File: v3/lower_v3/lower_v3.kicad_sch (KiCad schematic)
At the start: 4 parts, among them J1 Conn_01x09_MountingPin, J2 Conn_01x09_MountingPin, J4 Conn_01x02_Male, U1 ESP32-DEVKIT-V1

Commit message: Updates
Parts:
- added N1: Housing, Filter:Filter_1109-5_1.1x0.9mm, symbol Mechanical:Housing
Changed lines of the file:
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@@
     (pin "2")
+  )
+  (symbol (lib_id "Mechanical:Housing") (at 194.31 96.52 0) (unit 1)
+    (in_bom yes) (on_board yes) (fields_autoplaced)
+    (property "Reference" "N1" (id 0) (at 198.12 95.5674 0)
+      (effects (font (size 1.27 1.27)) (justify left))
+    )
+    (property "Value" "Housing" (id 1) (at 198.12 98.1074 0)
+      (effects (font (size 1.27 1.27)) (justify left))
+    )
+    (property "Footprint" "Filter:Filter_1109-5_1.1x0.9mm" (id 2) (at 195.58 95.25 0)
+      (effects (font (size 1.27 1.27)) hide)
+    )
+    (property "Datasheet" "~" (id 3) (at 195.58 95.25 0)
+      (effects (font (size 1.27 1.27)) hide)
+    )
   )
   (sheet_instances
@@
       (reference "J4") (unit 1) (value "Conn_01x02_Male") (footprint "Connector_PinHeader_2.54mm:PinHeader_1x02_P2.54mm_Vertical")
     )
+    (path "/b4f93f89-84ab-4a49-afa5-fdb220e94526"
+      (reference "N1") (unit 1) (value "Housing") (footprint "Filter:Filter_1109-5_1.1x0.9mm")
+    )
     (path "/821c0c0e-bb45-4cb0-9a8b-2228365f0032"

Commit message: Complete Toast PCB
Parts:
- removed J1, J2: Conn_01x09_MountingPin, Connector_PinSocket_2.54mm:PinSocket_1x09_P2.54mm_Vertical, symbol Connector_Generic_MountingPin:Conn_01x09_MountingPin
- added J1, J2: Conn_01x05_Male, Connector_PinHeader_2.54mm:PinHeader_1x05_P2.54mm_Vertical, symbol Connector:Conn_01x05_Male
- added J3: Conn_01x21, Connector_PinHeader_2.54mm:PinHeader_1x21_P2.54mm_Horizontal, symbol Connector_Generic:Conn_01x21
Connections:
- net GND: now also J4.2 (Pin_2), J2.1 (Pin_1), J3.12 (Pin_12), J3.15 (Pin_15), J3.18 (Pin_18), J3.21 (Pin_21), J3.3 (Pin_3), J3.6 (Pin_6), J3.9 (Pin_9); no longer J4.1 (Pin_1)
- net at U1.11 (D21): now also J1.1 (Pin_1)
- net at U1.10 (D19): now also J1.2 (Pin_2)
- net at U1.9 (D18): now also J1.3 (Pin_3)
- net at U1.8 (D5): now also J1.4 (Pin_4)
- net at U1.5 (D4): now also J2.4 (Pin_4)
- net at U1.4 (D2): now also J2.5 (Pin_5)
- net at U1.28 (D13): now also J2.2 (Pin_2)
- net at U1.27 (D12): now also J2.3 (Pin_3)
- net at U1.30 (VIN): now also J1.5 (Pin_5)
- net at U1.19 (D34): now also J3.19 (Pin_19)
- net at U1.20 (D35): now also J3.16 (Pin_16)
- net at U1.21 (D32): now also J3.13 (Pin_13)
- net at U1.22 (D33): now also J3.10 (Pin_10)
- net at U1.23 (D25): now also J3.7 (Pin_7)
- net at U1.25 (D27): now also J3.4 (Pin_4)
- net at U1.26 (D14): now also J3.1 (Pin_1)
- new net: J3.11 (Pin_11), J3.14 (Pin_14), J3.17 (Pin_17), J3.2 (Pin_2), J3.20 (Pin_20), J3.5 (Pin_5), J3.8 (Pin_8), J4.1 (Pin_1)
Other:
- moved on the sheet: J4, N1

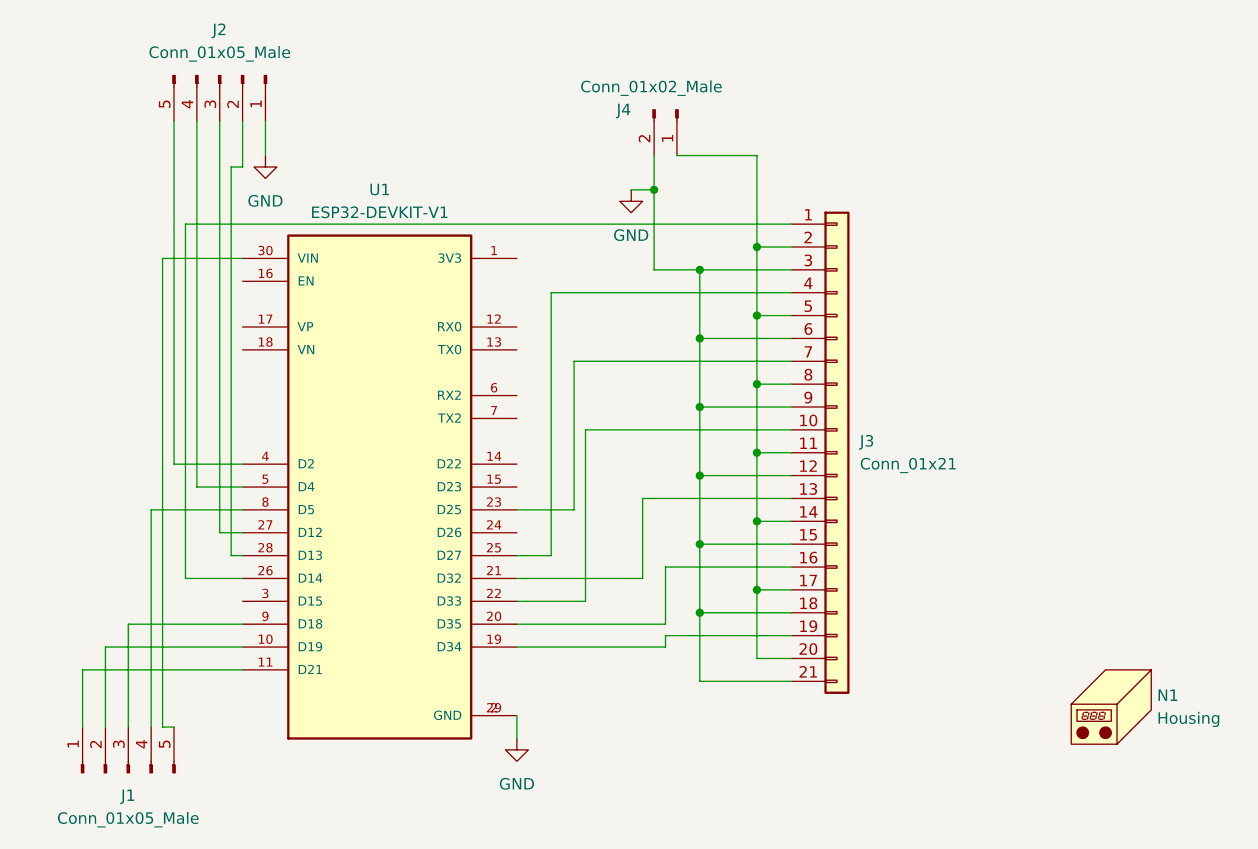
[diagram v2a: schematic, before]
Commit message: Adding clear Proto-board portion for the DOME
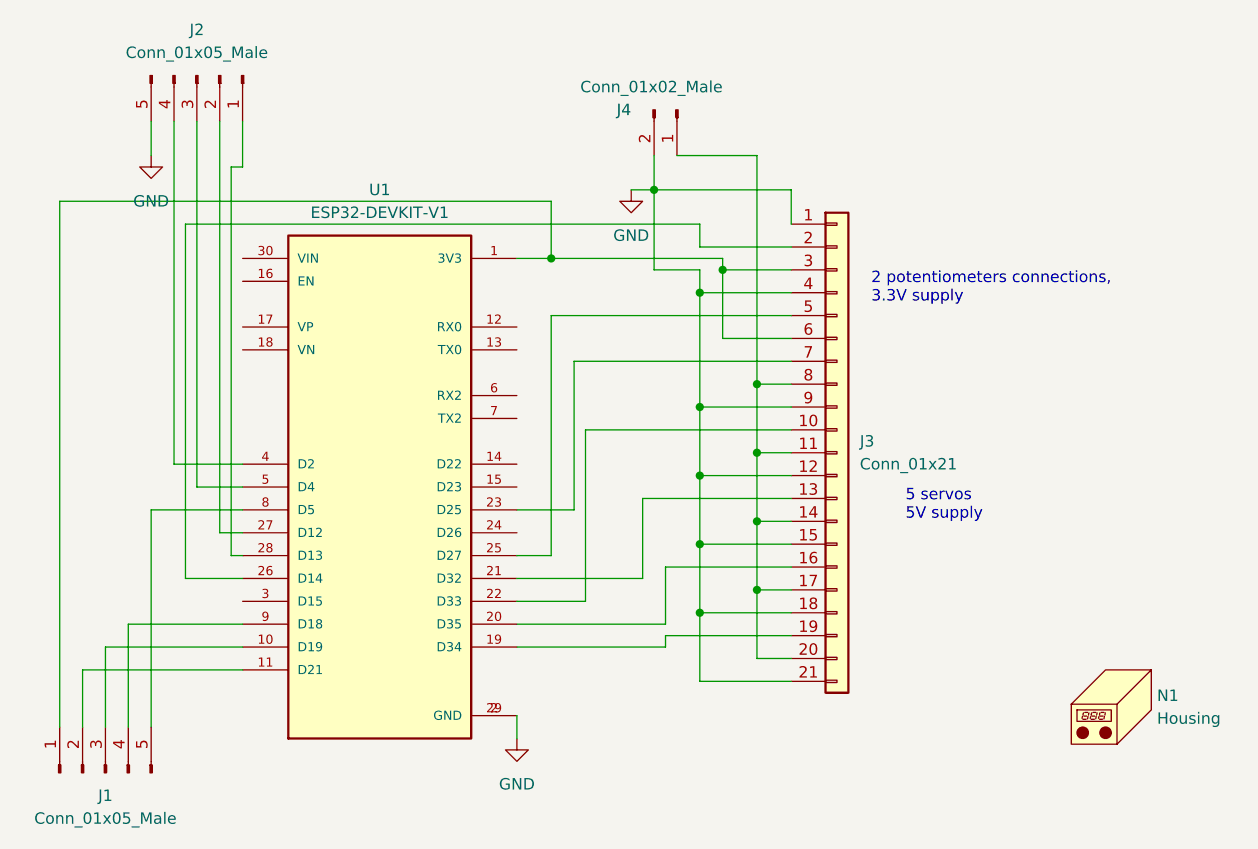
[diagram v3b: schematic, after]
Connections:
- net GND: now also J2.5 (Pin_5), J3.1 (Pin_1), J3.4 (Pin_4); no longer J2.1 (Pin_1), J3.3 (Pin_3), J3.6 (Pin_6)
- net at U1.28 (D13): now also J2.1 (Pin_1); no longer J2.2 (Pin_2)
- net at U1.27 (D12): now also J2.2 (Pin_2); no longer J2.3 (Pin_3)
- net at U1.5 (D4): now also J2.3 (Pin_3); no longer J2.4 (Pin_4)
- net at U1.4 (D2): now also J2.4 (Pin_4); no longer J2.5 (Pin_5)
- net at J1.1 (Pin_1): now also J3.3 (Pin_3), J3.6 (Pin_6), U1.1 (3V3); no longer U1.11 (D21)
- net at J1.2 (Pin_2): now also U1.11 (D21); no longer U1.10 (D19)
- net at J1.3 (Pin_3): now also U1.10 (D19); no longer U1.9 (D18)
- net at J1.4 (Pin_4): now also U1.9 (D18); no longer U1.8 (D5)
- net at J1.5 (Pin_5): now also U1.8 (D5); no longer U1.30 (VIN)
- net at U1.26 (D14): now also J3.2 (Pin_2); no longer J3.1 (Pin_1)
- net at J3.11 (Pin_11), J3.14 (Pin_14), J3.17 (Pin_17)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: no longer J3.2 (Pin_2), J3.5 (Pin_5)
- net at U1.25 (D27): now also J3.5 (Pin_5); no longer J3.4 (Pin_4)
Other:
- note added: "2 potentiometers connections, 3.3V supply"
- note added: "5 servos 5V supply"
- moved on the sheet: J1, J2

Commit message: Rev.A Toast Design, fixing connection between 2 boards, adding 3 I/O for the DOME, creating blank proto area for testing
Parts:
- removed J2: Conn_01x05_Male, Connector_PinHeader_2.54mm:PinHeader_1x05_P2.54mm_Vertical, symbol Connector:Conn_01x05_Male
- added J2: Conn_01x06_Male, Connector_PinHeader_2.54mm:PinHeader_1x06_P2.54mm_Vertical, symbol Connector:Conn_01x06_Male
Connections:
- net GND: now also J2.6 (Pin_6)
- net at U1.28 (D13): now also J2.2 (Pin_2)
- net at U1.27 (D12): now also J2.3 (Pin_3)
- net at U1.5 (D4): now also J2.4 (Pin_4)
- net at U1.4 (D2): now also J2.5 (Pin_5)
- net at J3.11 (Pin_11), J3.14 (Pin_14), J3.17 (Pin_17)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: now also J2.1 (Pin_1)
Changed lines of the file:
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@@
   (junction (at 181.61 97.79) (diameter 0) (color 0 0 0 0)
   )
+  (junction (at 179.07 62.23) (diameter 0) (color 0 0 0 0)
+  )
   (junction (at 187.96 87.63) (diameter 0) (color 0 0 0 0)
   )
@@
     (stroke (width 0) (type default) (color 0 0 0 0))
   )
+  (wire (pts (xy 179.07 62.23) (xy 179.07 63.5))
+    (stroke (width 0) (type default) (color 0 0 0 0))
+  )
   (wire (pts (xy 165.1 80.01) (xy 191.77 80.01))
     (stroke (width 0) (type default) (color 0 0 0 0))
@@
     (stroke (width 0) (type default) (color 0 0 0 0))
   )
+  (wire (pts (xy 179.07 63.5) (xy 133.35 63.5))
+    (stroke (width 0) (type default) (color 0 0 0 0))
+  )
   (wire (pts (xy 181.61 90.17) (xy 191.77 90.17))
     (stroke (width 0) (type default) (color 0 0 0 0))
@@
   )
   (wire (pts (xy 165.1 80.01) (xy 165.1 106.68))
+    (stroke (width 0) (type default) (color 0 0 0 0))
+  )
+  (wire (pts (xy 133.35 63.5) (xy 133.35 58.42))
     (stroke (width 0) (type default) (color 0 0 0 0))
   )
@@
     )
     (pin "1")
-  )
-  (symbol (lib_id "Connector:Conn_01x05_Male") (at 125.73 53.34 270) (unit 1)
-    (in_bom yes) (on_board yes) (fields_autoplaced)
-    (property "Reference" "J2" (id 0) (at 125.73 48.26 90))
-    (property "Value" "Conn_01x05_Male" (id 1) (at 125.73 50.8 90))
-    (property "Footprint" "Connector_PinHeader_2.54mm:PinHeader_1x05_P2.54mm_Vertical" (id 2) (at 125.73 53.34 0)
-      (effects (font (size 1.27 1.27)) hide)
-    )
-    (property "Datasheet" "~" (id 3) (at 125.73 53.34 0)
-      (effects (font (size 1.27 1.27)) hide)
-    )
-    (pin "1")
-    (pin "2")
-    (pin "3")
-    (pin "4")
-    (pin "5")
   )
   (symbol (lib_id "power:GND") (at 173.99 66.04 0) (unit 1)
@@
     (pin "8")
     (pin "9")
+  )
+  (symbol (lib_id "Connector:Conn_01x06_Male") (at 128.27 53.34 270) (unit 1)
+    (in_bom yes) (on_board yes) (fields_autoplaced)
+    (property "Reference" "J2" (id 0) (at 127 48.26 90))
+    (property "Value" "Conn_01x06_Male" (id 1) (at 127 50.8 90))
+    (property "Footprint" "Connector_PinHeader_2.54mm:PinHeader_1x06_P2.54mm_Vertical" (id 2) (at 128.27 53.34 0)
+      (effects (font (size 1.27 1.27)) hide)
+    )
+    (property "Datasheet" "~" (id 3) (at 128.27 53.34 0)
+      (effects (font (size 1.27 1.27)) hide)
+    )
+    (pin "1")
+    (pin "2")
+    (pin "3")
+    (pin "4")
+    (pin "5")
+    (pin "6")
   )
   (symbol (lib_id "ESP32-DEVKIT-V1:ESP32-DEVKIT-V1") (at 146.05 99.06 0) (unit 1)
@@
       (reference "J1") (unit 1) (value "Conn_01x05_Male") (footprint "Connector_PinHeader_2.54mm:PinHeader_1x05_P2.54mm_Vertical")
     )
-    (path "/1c2daf2c-b78e-4025-804d-a3ba4f42c959"
-      (reference "J2") (unit 1) (value "Conn_01x05_Male") (footprint "Connector_PinHeader_2.54mm:PinHeader_1x05_P2.54mm_Vertical")
+    (path "/6d6a81f1-0654-4a08-8ee5-21fbf1be7314"
+      (reference "J2") (unit 1) (value "Conn_01x06_Male") (footprint "Connector_PinHeader_2.54mm:PinHeader_1x06_P2.54mm_Vertical")
     )
     (path "/4954e726-41d3-489a-a47a-026c6de8b6f6"

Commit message: With OshPark order
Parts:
- removed N1: Housing, Filter:Filter_1109-5_1.1x0.9mm, symbol Mechanical:Housing
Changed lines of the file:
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@@
     (pin "2")
-  )
-  (symbol (lib_id "Mechanical:Housing") (at 228.6 123.19 0) (unit 1)
-    (in_bom yes) (on_board yes) (fields_autoplaced)
-    (property "Reference" "N1" (id 0) (at 232.41 122.2374 0)
-      (effects (font (size 1.27 1.27)) (justify left))
-    )
-    (property "Value" "Housing" (id 1) (at 232.41 124.7774 0)
-      (effects (font (size 1.27 1.27)) (justify left))
-    )
-    (property "Footprint" "Filter:Filter_1109-5_1.1x0.9mm" (id 2) (at 229.87 121.92 0)
-      (effects (font (size 1.27 1.27)) hide)
-    )
-    (property "Datasheet" "~" (id 3) (at 229.87 121.92 0)
-      (effects (font (size 1.27 1.27)) hide)
-    )
   )
   (sheet_instances
@@
       (reference "J4") (unit 1) (value "Conn_01x02_Male") (footprint "Connector_PinHeader_2.54mm:PinHeader_1x02_P2.54mm_Vertical")
     )
-    (path "/b4f93f89-84ab-4a49-afa5-fdb220e94526"
-      (reference "N1") (unit 1) (value "Housing") (footprint "Filter:Filter_1109-5_1.1x0.9mm")
-    )
     (path "/821c0c0e-bb45-4cb0-9a8b-2228365f0032"

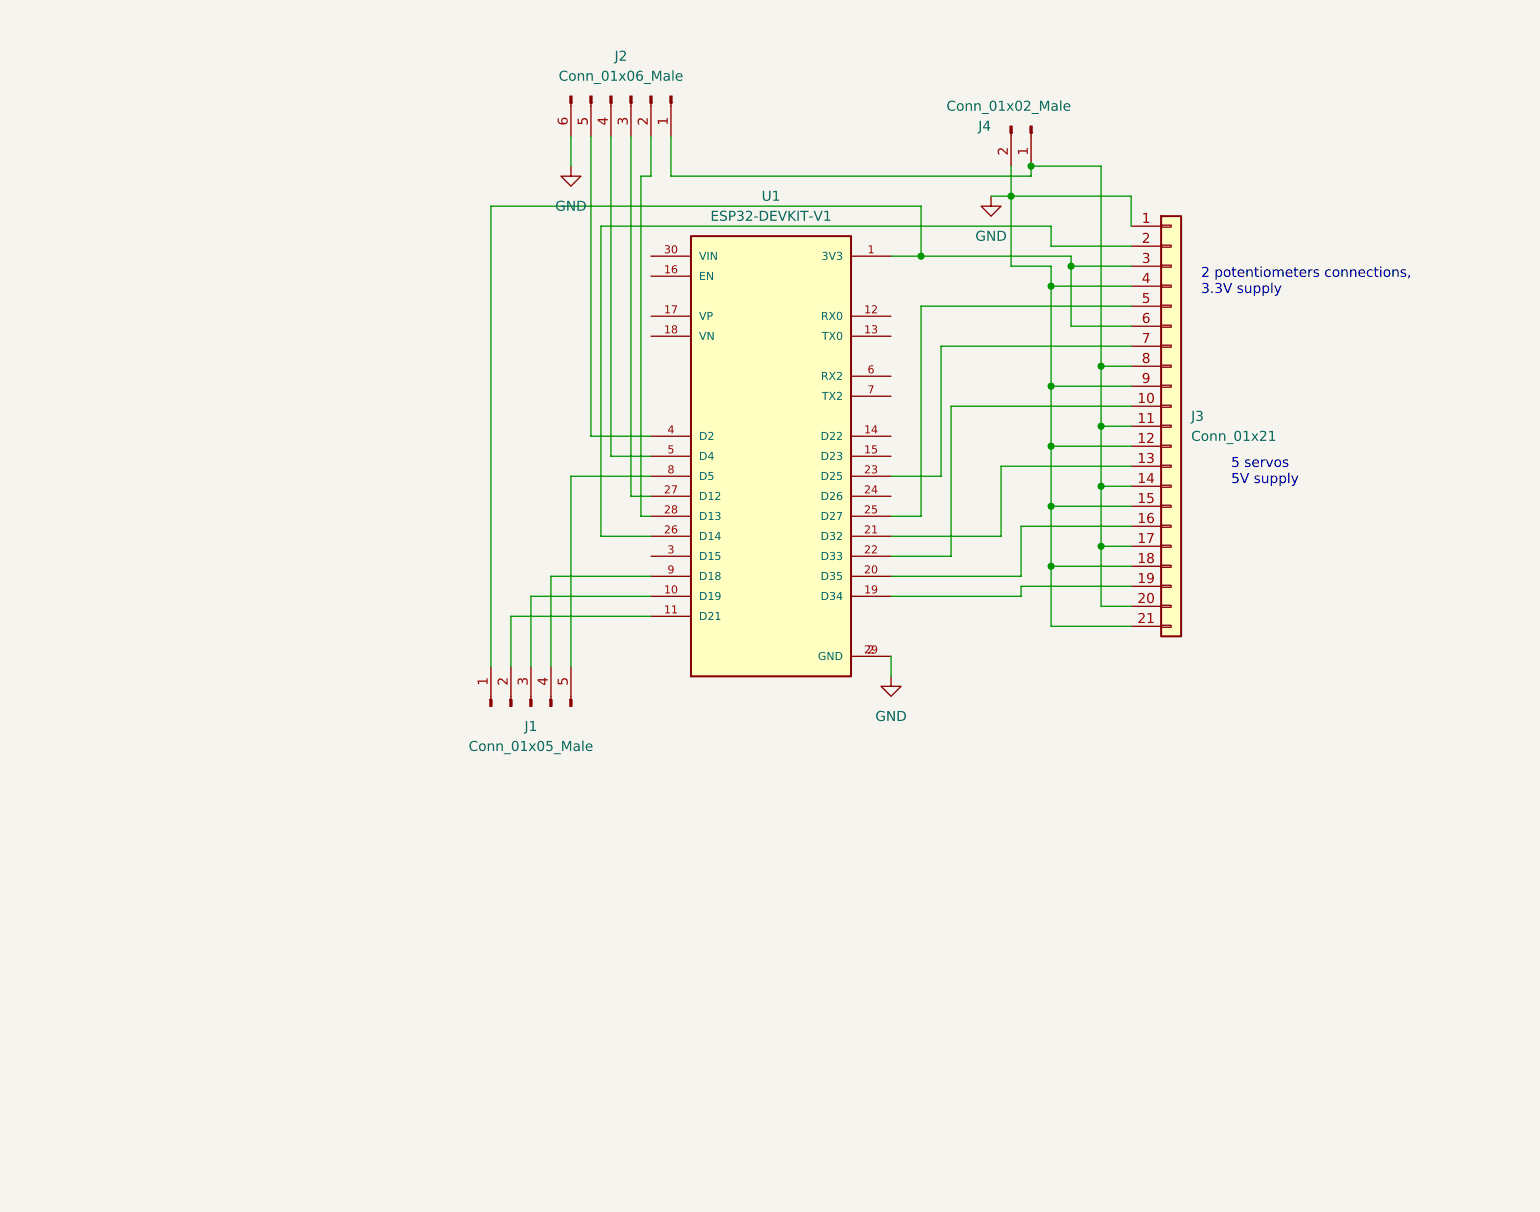
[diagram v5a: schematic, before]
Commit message: Lay out protoboard PCB
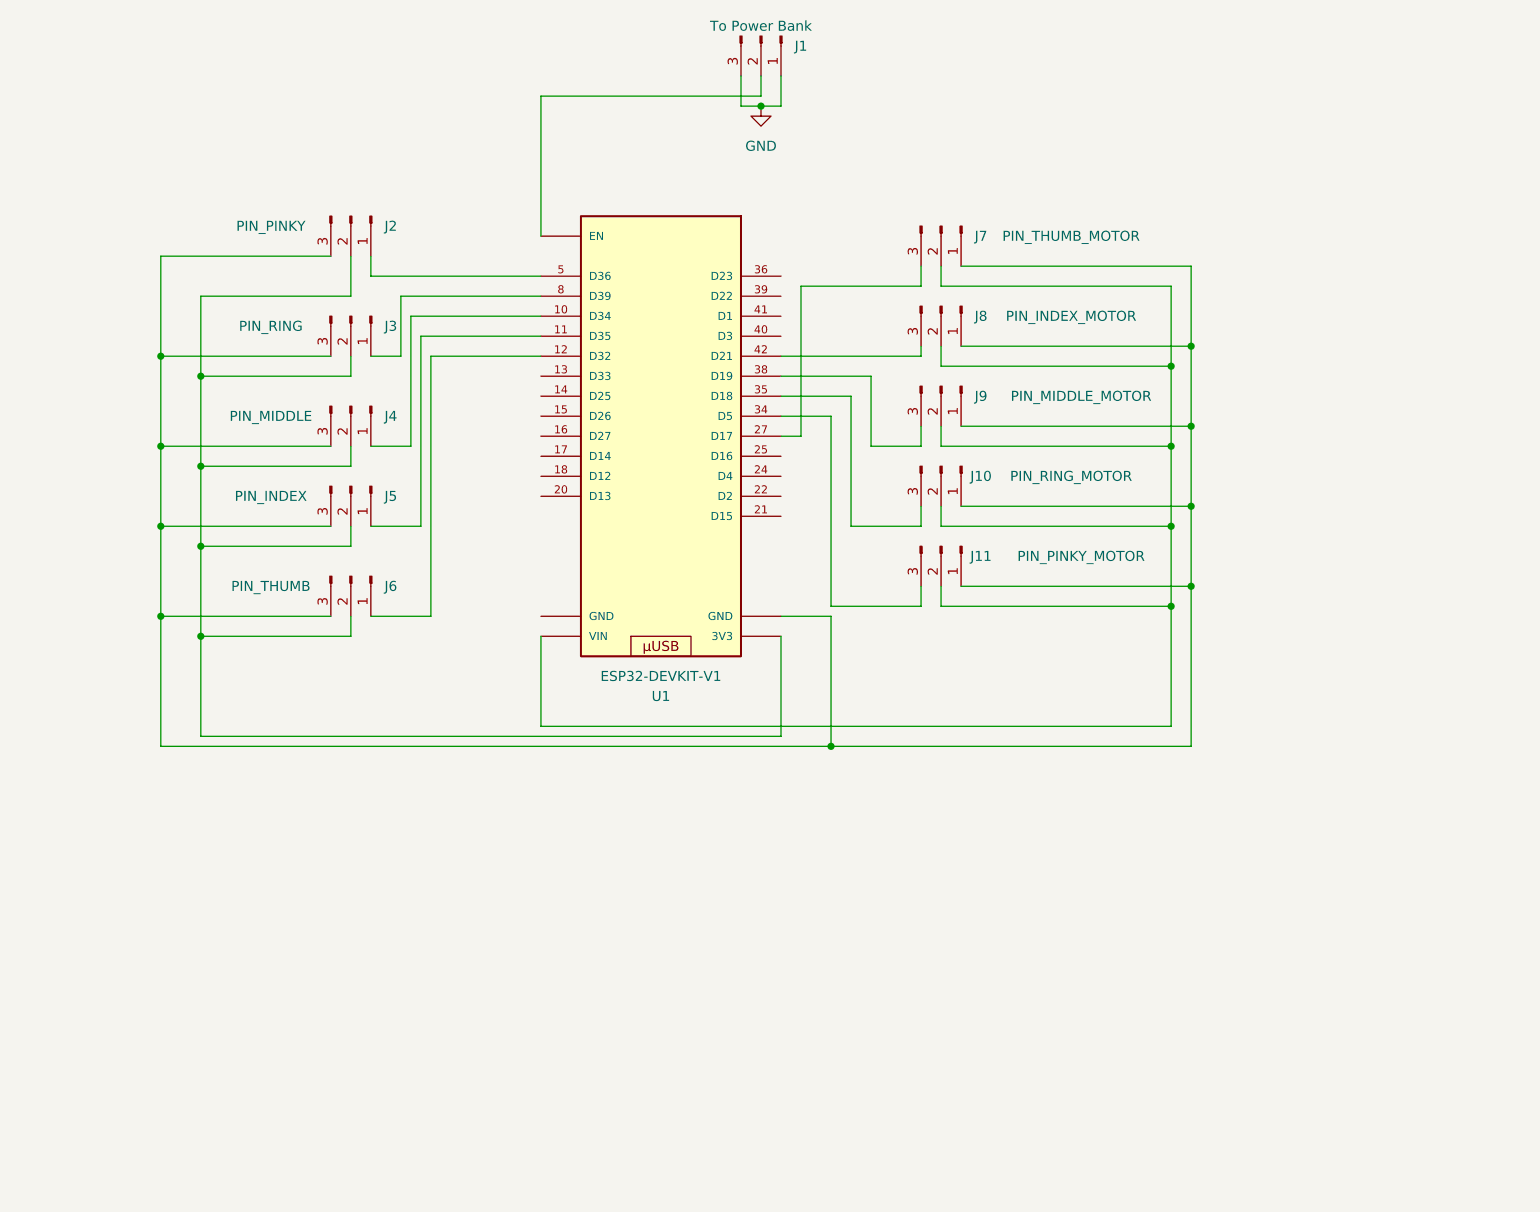
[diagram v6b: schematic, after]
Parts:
- removed J1: Conn_01x05_Male, Connector_PinHeader_2.54mm:PinHeader_1x05_P2.54mm_Vertical, symbol Connector:Conn_01x05_Male
- removed J2: Conn_01x06_Male, Connector_PinHeader_2.54mm:PinHeader_1x06_P2.54mm_Vertical, symbol Connector:Conn_01x06_Male
- removed J3: Conn_01x21, Connector_PinHeader_2.54mm:PinHeader_1x21_P2.54mm_Horizontal, symbol Connector_Generic:Conn_01x21
- removed J4: Conn_01x02_Male, Connector_PinHeader_2.54mm:PinHeader_1x02_P2.54mm_Vertical, symbol Connector:Conn_01x02_Male
- added J1: To Power Bank, symbol Connector:Conn_01x03_Male
- added J10: PIN_RING_MOTOR, symbol Connector:Conn_01x03_Male
- added J11: PIN_PINKY_MOTOR, symbol Connector:Conn_01x03_Male
- added J2: PIN_PINKY, symbol Connector:Conn_01x03_Male
- added J3: PIN_RING, symbol Connector:Conn_01x03_Male
- added J4: PIN_MIDDLE, symbol Connector:Conn_01x03_Male
- added J5: PIN_INDEX, symbol Connector:Conn_01x03_Male
- added J6: PIN_THUMB, symbol Connector:Conn_01x03_Male
- added J7: PIN_THUMB_MOTOR, symbol Connector:Conn_01x03_Male
- added J8: PIN_INDEX_MOTOR, symbol Connector:Conn_01x03_Male
- added J9: PIN_MIDDLE_MOTOR, symbol Connector:Conn_01x03_Male
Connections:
- net GND: now also J1.1 (Pin_1), J1.3 (Pin_3); no longer U1.2 (GND), U1.29 (GND)
- net at U1.11 (D35): now also J5.1 (Pin_1)
- net at U1.10 (D34): now also J4.1 (Pin_1)
- net at U1.8 (D39): now also J3.1 (Pin_1)
- net at U1.27 (D17): now also J7.3 (Pin_3)
- net at U1.5 (D36): now also J2.1 (Pin_1)
- net at U1.12 (D32): now also J6.1 (Pin_1)
- new net: J2.2 (Pin_2), J3.2 (Pin_2), J4.2 (Pin_2), J5.2 (Pin_2), J6.2 (Pin_2), U1. (VIN)
- new net: J10.1 (Pin_1), J11.1 (Pin_1), J2.3 (Pin_3), J3.3 (Pin_3), J4.3 (Pin_3), J5.3 (Pin_3), J6.3 (Pin_3), J7.1 (Pin_1), J8.1 (Pin_1), J9.1 (Pin_1), U1. (VIN)
- new net: J10.2 (Pin_2), J11.2 (Pin_2), J7.2 (Pin_2), J8.2 (Pin_2), J9.2 (Pin_2), U1. (VIN)
- new net: J11.3 (Pin_3), U1.34 (D5)
- new net: J1.2 (Pin_2), U1. (VIN)
- new net: J10.3 (Pin_3), U1.35 (D18)
- new net: J9.3 (Pin_3), U1.38 (D19)
- new net: J8.3 (Pin_3), U1.42 (D21)
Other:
- note removed: "2 potentiometers connections, 3.3V supply"
- note removed: "5 servos 5V supply"
